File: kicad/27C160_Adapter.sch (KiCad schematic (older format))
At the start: 10 parts, among them Q1 BC327, SW1 MS22D16, SW2 DIP, U1 27C4002

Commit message: Changed dip switch to coded rotary switch. Still needs rerouting.
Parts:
- removed SW2: DIP, 27C160_Adapter:EDG-03, symbol SW_DIP-3
- added SW2: 94HBB08T, 27C160_Adapter:94HBB08T, symbol 94HBB08T
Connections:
- wire segments 119 -> 117

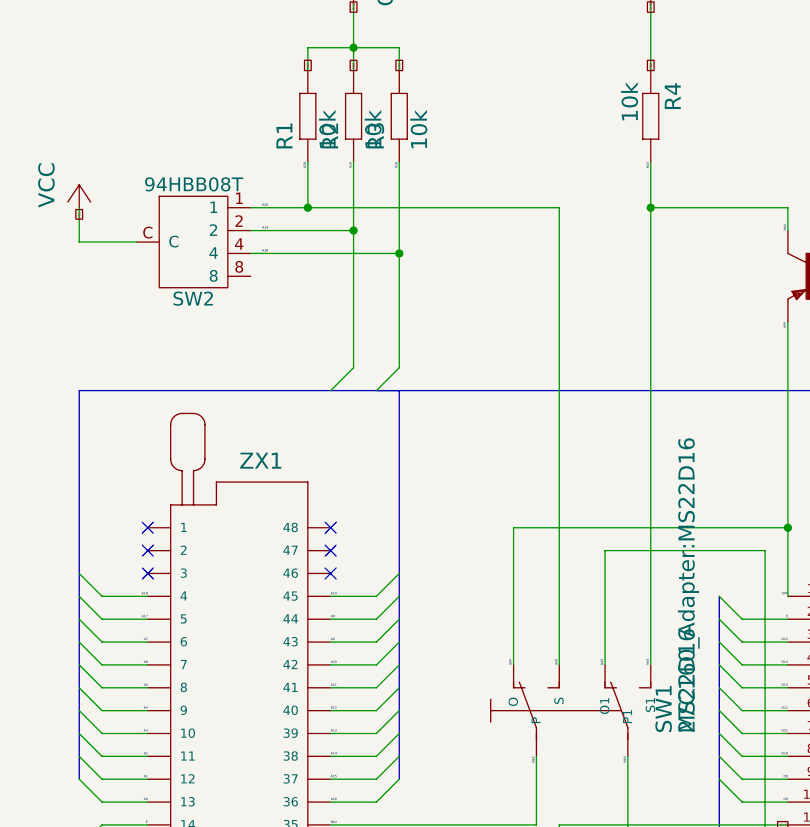
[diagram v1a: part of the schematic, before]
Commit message: Hotfix for LSB error
Whoops! had my LSB and MSB swapped. That would have given some undesired
behavior.
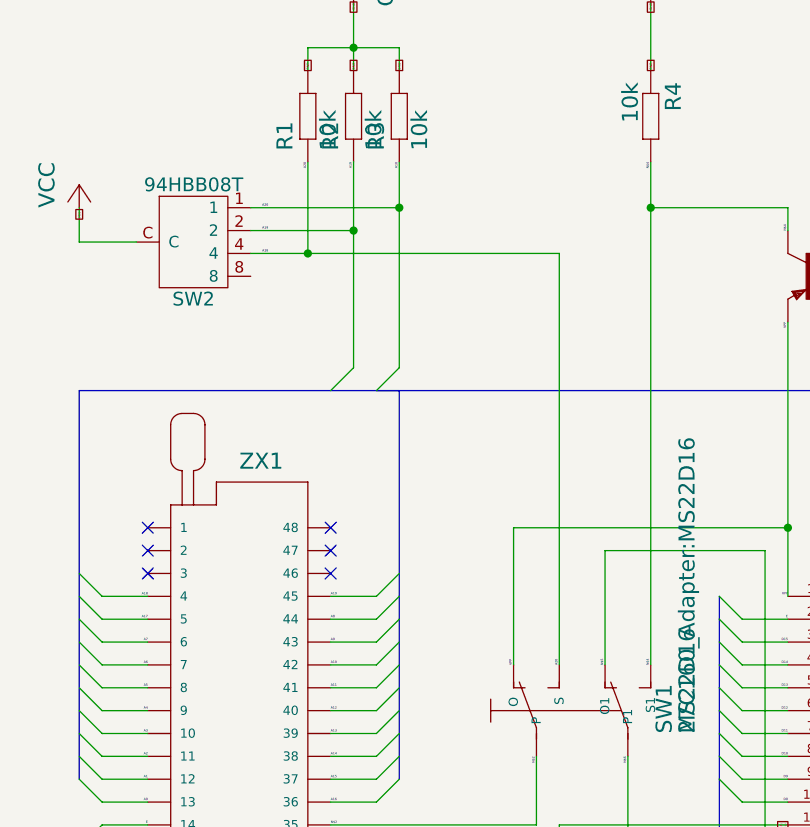
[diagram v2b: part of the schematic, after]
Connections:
- net A20 is gone; now on net A18: R1.1, SW1.3 (S), SW2.1

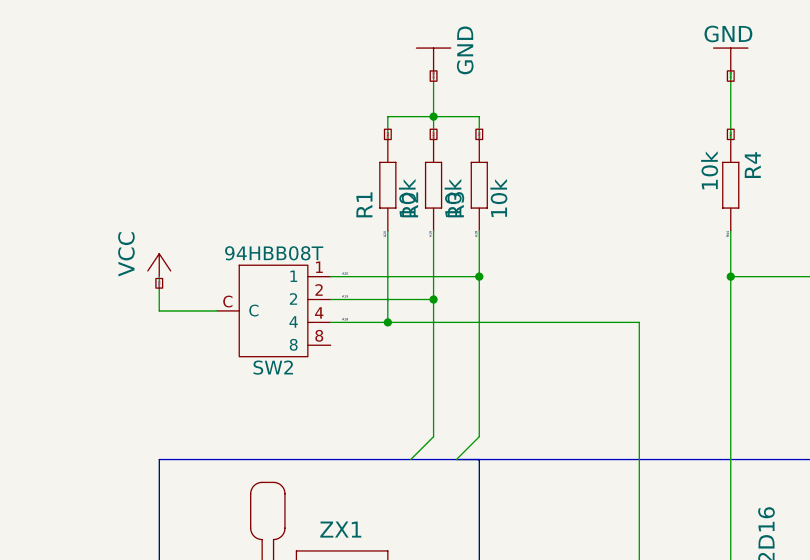
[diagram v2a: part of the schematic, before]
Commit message: Actual fix for LSB/MSB mixup
Had actually only rearranged the pulldown resistors. Which doesn't
actually do anything at all. Let this be a lesson: if you make a
correction at 2AM, check it before you send it to the fab house. Fixes
Issue #1 .
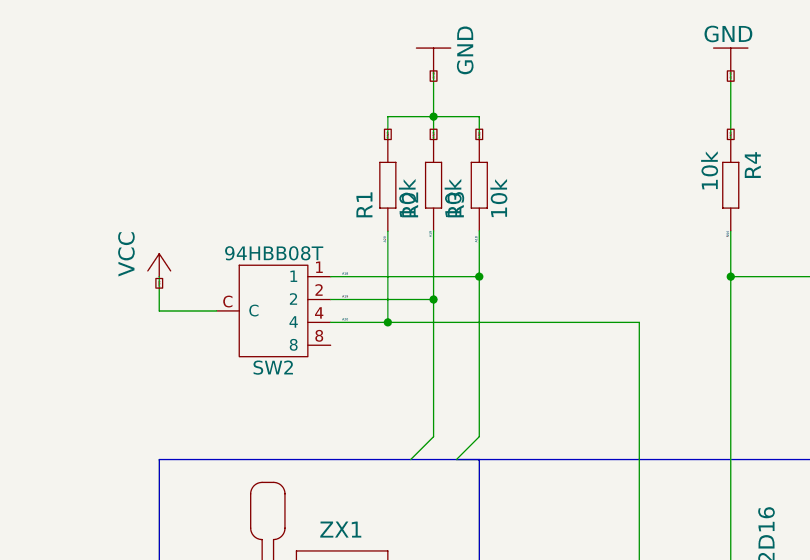
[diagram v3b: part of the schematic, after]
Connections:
- net A18: no longer R1.1, SW1.3 (S), SW2.4
- new net A20: R1.1, SW1.3 (S), SW2.4
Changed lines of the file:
@@
 Text Label 8950 7300 2    10   ~ 0
-A18
-Text Label 9450 5800 0    10   ~ 0
-A18
-Text Label 10050 5400 3    10   ~ 0
 A18
 Text Label 9750 7300 0    10   ~ 0
@@
 Text Label 9850 5400 3    10   ~ 0
 A19
-Text Label 9450 5600 0    10   ~ 0
-A20
-Text Label 9650 5400 3    10   ~ 0
-A20
 Text Label 10750 7600 1    10   ~ 0
 A20
@@
 	8950 7300 8750 7300
 Wire Wire Line
-	10050 5400 10050 6300
-Wire Wire Line
-	10050 6300 9950 6400
-Wire Wire Line
 	9750 7300 9950 7300
 Wire Wire Line
@@
 Connection ~ 9850 5700
 Wire Wire Line
-	9650 5800 9650 5400
-Wire Wire Line
 	10750 5800 10750 7600
-Connection ~ 9650 5800
 Wire Wire Line
 	8950 8600 8750 8600
@@
 	13250 6400 13250 9100
 Wire Bus Line
+	8650 8400 8650 9600
+Wire Bus Line
+	8650 9600 11450 9600
+Wire Bus Line
+	11450 9600 11450 7300
+Wire Bus Line
+	10050 8600 10050 9600
+Wire Wire Line
+	8900 5750 8650 5750
+Wire Wire Line
+	8650 5750 8650 5600
+Wire Bus Line
+	10050 6400 10050 8100
+Wire Bus Line
 	9950 6400 10050 6400
-Wire Bus Line
-	10050 6400 10050 8100
-Wire Bus Line
-	8650 8400 8650 9600
-Wire Bus Line
-	8650 9600 11450 9600
-Wire Bus Line
-	11450 9600 11450 7300
-Wire Bus Line
-	10050 8600 10050 9600
-Wire Wire Line
-	8900 5750 8650 5750
-Wire Wire Line
-	8650 5750 8650 5600
+Wire Wire Line
+	10050 6300 9950 6400
+Wire Wire Line
+	10050 5400 10050 6300
+Wire Wire Line
+	9650 5400 9650 5800
 Wire Wire Line
 	9400 5800 10750 5800
-Wire Wire Line
-	10050 5600 9400 5600
+Text Label 9450 5800 0    10   ~ 0
+A20
+Text Label 9650 5450 1    10   ~ 0
+A20
+Connection ~ 9650 5800
+Wire Wire Line
+	9400 5600 10050 5600
 Connection ~ 10050 5600
+Text Label 10050 5450 1    10   ~ 0
+A18
+Text Label 9450 5600 0    10   ~ 0
+A18
 $EndSCHEMATC
